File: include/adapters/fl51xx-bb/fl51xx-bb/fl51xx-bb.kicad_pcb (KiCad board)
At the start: 2 copper layers, 93.3 x 97.3 mm, 90 parts, among them J1 Conn_01x05, J2 Conn_01x05, U1 FL51xxMX

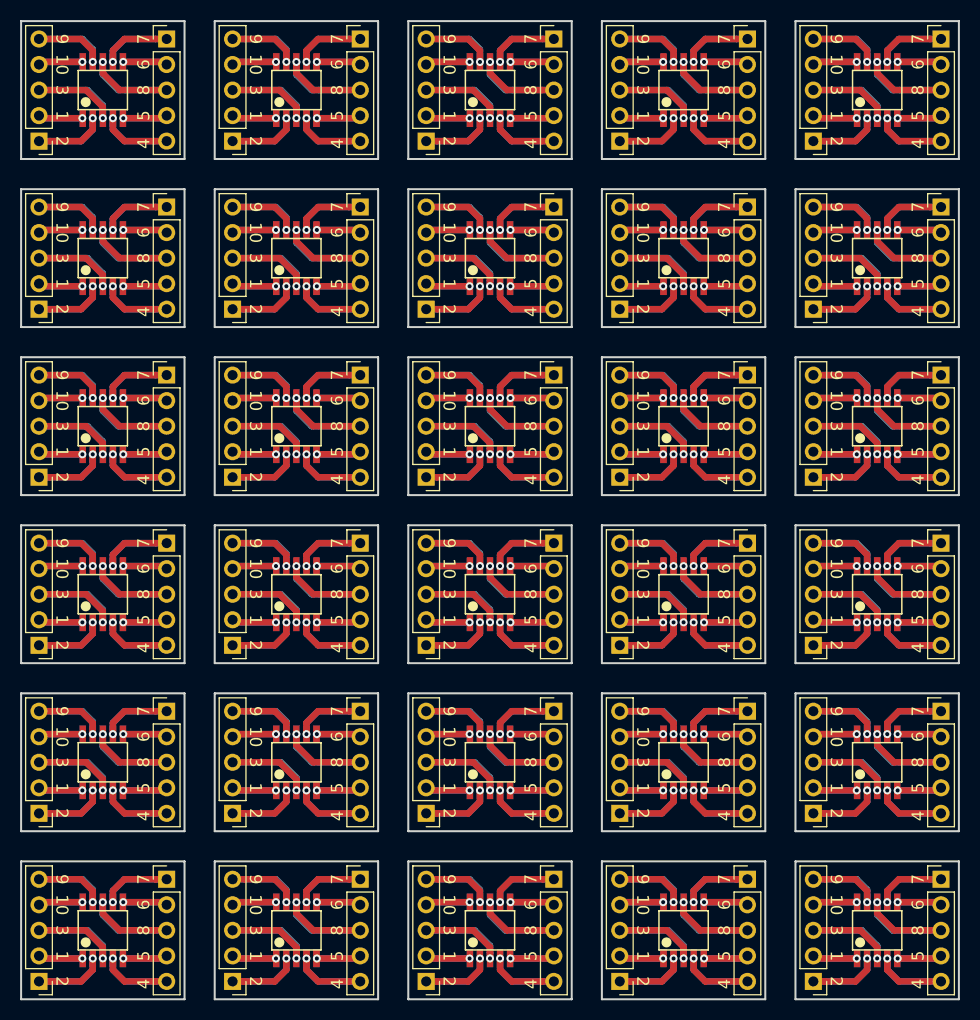
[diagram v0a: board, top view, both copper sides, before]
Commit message: removed duplicates
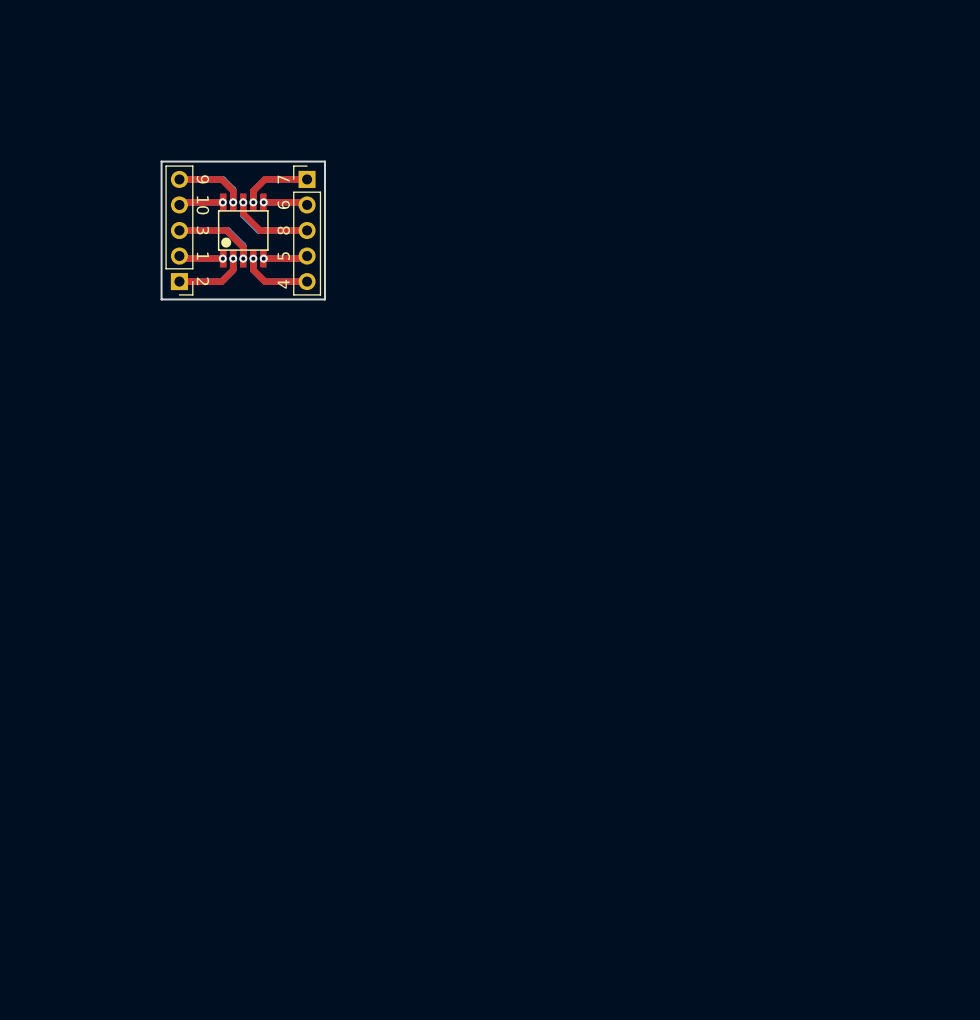
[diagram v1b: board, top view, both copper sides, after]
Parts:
- removed the J1 at (78.8, 95.5)
- removed the J1 at (1.78, 78.8)
- removed the J1 at (78.8, 62.1)
- removed the J1 at (59.5, 62.1)
- removed the J1 at (40.3, 62.1)
- removed the J1 at (21.0, 62.1)
- removed the J1 at (1.78, 62.1)
- removed the J1 at (78.8, 45.4)
- removed the J1 at (59.5, 45.4)
- removed the J1 at (40.3, 45.4)
- removed the J1 at (21.0, 45.4)
- removed the J1 at (59.5, 95.5)
- removed the J1 at (1.78, 45.4)
- removed the J1 at (78.8, 28.7)
- removed the J1 at (59.5, 28.7)
- removed the J1 at (40.3, 28.7)
- removed the J1 at (21.0, 28.7)
- removed the J1 at (1.78, 28.7)
- removed the J1 at (78.8, 11.9)
- removed the J1 at (59.5, 11.9)
- removed the J1 at (40.3, 11.9)
- removed the J1 at (21.0, 11.9)
- removed the J1 at (40.3, 95.5)
- removed the J1 at (21.0, 95.5)
- removed the J1 at (1.78, 95.5)
- removed the J1 at (78.8, 78.8)
- removed the J1 at (59.5, 78.8)
- removed the J1 at (40.3, 78.8)
- removed the J1 at (21.0, 78.8)
- removed the J2 at (91.5, 85.4)
- removed the J2 at (14.5, 68.6)
- removed the J2 at (91.5, 51.9)
- removed the J2 at (72.2, 51.9)
- removed the J2 at (53.0, 51.9)
- removed the J2 at (33.7, 51.9)
- removed the J2 at (14.5, 51.9)
- removed the J2 at (91.5, 35.2)
- removed the J2 at (72.2, 35.2)
- removed the J2 at (53.0, 35.2)
- removed the J2 at (33.7, 35.2)
- removed the J2 at (72.2, 85.4)
- removed the J2 at (14.5, 35.2)
- removed the J2 at (91.5, 18.5)
- removed the J2 at (72.2, 18.5)
- removed the J2 at (53.0, 18.5)
- removed the J2 at (33.7, 18.5)
- removed the J2 at (14.5, 18.5)
- removed the J2 at (91.5, 1.78)
- removed the J2 at (72.2, 1.78)
- removed the J2 at (53.0, 1.78)
- removed the J2 at (33.7, 1.78)
- removed the J2 at (53.0, 85.4)
- removed the J2 at (33.7, 85.4)
- removed the J2 at (14.5, 85.4)
- removed the J2 at (91.5, 68.6)
- removed the J2 at (72.2, 68.6)
- removed the J2 at (53.0, 68.6)
- removed the J2 at (33.7, 68.6)
- removed the U1 at (85.2, 90.4)
- removed the U1 at (8.13, 73.7)
- removed the U1 at (85.2, 57.0)
- removed the U1 at (65.9, 57.0)
- removed the U1 at (46.6, 57.0)
- removed the U1 at (27.4, 57.0)
- removed the U1 at (8.13, 57.0)
- removed the U1 at (85.2, 40.3)
- removed the U1 at (65.9, 40.3)
- removed the U1 at (46.6, 40.3)
- removed the U1 at (27.4, 40.3)
- removed the U1 at (65.9, 90.4)
- removed the U1 at (8.13, 40.3)
- removed the U1 at (85.2, 23.6)
- removed the U1 at (65.9, 23.6)
- removed the U1 at (46.6, 23.6)
- removed the U1 at (27.4, 23.6)
- removed the U1 at (8.13, 23.6)
- removed the U1 at (85.2, 6.86)
- removed the U1 at (65.9, 6.86)
- removed the U1 at (46.6, 6.86)
- removed the U1 at (27.4, 6.86)
- removed the U1 at (46.6, 90.4)
- removed the U1 at (27.4, 90.4)
- removed the U1 at (8.13, 90.4)
- removed the U1 at (85.2, 73.7)
- removed the U1 at (65.9, 73.7)
- removed the U1 at (46.6, 73.7)
- removed the U1 at (27.4, 73.7)
- moved J1 19.8 mm to (15.7, 25.9)
- moved J2 19.8 mm to (28.4, 15.7)
- moved U1 19.8 mm to (22.1, 20.8)
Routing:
- net Net-(J1-Pad3): track 516.2 -> 17.2 mm, vias 30 -> 1
- net Net-(J2-Pad3): track 492.6 -> 16.4 mm, vias 30 -> 1
- net Net-(J1-Pad5): track 419.4 -> 14.0 mm, vias 30 -> 1
- net Net-(J2-Pad5): track 417.2 -> 13.9 mm, vias 30 -> 1
- net Net-(J2-Pad1): track 417.2 -> 13.9 mm, vias 30 -> 1
- net Net-(J1-Pad1): track 417.2 -> 13.9 mm, vias 30 -> 1
- net Net-(J2-Pad4): track 266.5 -> 8.88 mm, vias 30 -> 1
- net Net-(J1-Pad2): track 266.5 -> 8.88 mm, vias 30 -> 1
- net Net-(J1-Pad4): track 266.5 -> 8.88 mm, vias 30 -> 1
- net Net-(J2-Pad2): track 266.5 -> 8.88 mm, vias 30 -> 1
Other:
- board size 93.3 x 97.3 mm -> 16.3 x 13.7 mm

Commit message: first order
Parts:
- added J10: Conn_01x01, Connector_PinHeader_2.54mm:PinHeader_1x01_P2.54mm_Vertical, F.Cu at (31.5, 20.1)
- added J3: Conn_01x01, Connector_PinHeader_2.54mm:PinHeader_1x01_P2.54mm_Vertical, F.Cu at (18.8, 22.6)
- added J4: Conn_01x01, Connector_PinHeader_2.54mm:PinHeader_1x01_P2.54mm_Vertical, F.Cu at (31.5, 27.7)
- added J5: Conn_01x01, Connector_PinHeader_2.54mm:PinHeader_1x01_P2.54mm_Vertical, F.Cu at (31.5, 25.1)
- added J6: Conn_01x01, Connector_PinHeader_2.54mm:PinHeader_1x01_P2.54mm_Vertical, F.Cu at (18.8, 20.1)
- added J7: Conn_01x01, Connector_PinHeader_2.54mm:PinHeader_1x01_P2.54mm_Vertical, F.Cu at (18.8, 17.5)
- added J8: Conn_01x01, Connector_PinHeader_2.54mm:PinHeader_1x01_P2.54mm_Vertical, F.Cu at (31.5, 22.6)
- added J9: Conn_01x01, Connector_PinHeader_2.54mm:PinHeader_1x01_P2.54mm_Vertical, F.Cu at (31.5, 17.5)
- J1, J2: value Conn_01x05 -> Conn_01x01; footprint Connector_PinHeader_2.54mm:PinHeader_1x05_P2.54mm_Vertical -> Connector_PinHeader_2.54mm:PinHeader_1x01_P2.54mm_Vertical
- moved J2 15.4 mm to (18.8, 27.7)
- moved U1 3.53 mm to (25.1, 22.6)
- moved J1 3.14 mm to (18.8, 25.1), turned to 0 degrees
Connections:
- U1 pad 1: Net-(J1-Pad2) -> Net-(J1-Pad1)
- U1 pad 10: Net-(J1-Pad4) -> Net-(J6-Pad1)
- U1 pad 2: Net-(J1-Pad1) -> Net-(J2-Pad1)
- U1 pad 3: Net-(J1-Pad3) -> Net-(J3-Pad1)
- U1 pad 4: Net-(J2-Pad5) -> Net-(J4-Pad1)
- U1 pad 5: Net-(J2-Pad4) -> Net-(J5-Pad1)
- U1 pad 6: Net-(J2-Pad2) -> Net-(J10-Pad1)
- U1 pad 7: Net-(J2-Pad1) -> Net-(J9-Pad1)
- U1 pad 8: Net-(J2-Pad3) -> Net-(J8-Pad1)
- U1 pad 9: Net-(J1-Pad5) -> Net-(J7-Pad1)
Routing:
- net Net-(J3-Pad1): track 0.00 -> 17.3 mm, vias 0 -> 1
- net Net-(J1-Pad3): track 17.2 -> 0.00 mm, vias 1 -> 0
- net Net-(J8-Pad1): track 0.00 -> 16.5 mm, vias 0 -> 1
- net Net-(J2-Pad3): track 16.4 -> 0.00 mm, vias 1 -> 0
- net Net-(J7-Pad1): track 0.00 -> 15.0 mm, vias 0 -> 1
- net Net-(J1-Pad5): track 14.0 -> 0.00 mm, vias 1 -> 0
- net Net-(J2-Pad5): track 13.9 -> 0.00 mm, vias 1 -> 0
- net Net-(J9-Pad1): track 0.00 -> 13.9 mm, vias 0 -> 1
- net Net-(J4-Pad1): track 0.00 -> 13.9 mm, vias 0 -> 1
- net Net-(J2-Pad4): track 8.88 -> 0.00 mm, vias 1 -> 0
- net Net-(J2-Pad2): track 8.88 -> 0.00 mm, vias 1 -> 0
- net Net-(J1-Pad4): track 8.88 -> 0.00 mm, vias 1 -> 0
- net Net-(J1-Pad2): track 8.88 -> 0.00 mm, vias 1 -> 0
- net Net-(J6-Pad1): track 0.00 -> 8.88 mm, vias 0 -> 1
- net Net-(J5-Pad1): track 0.00 -> 8.88 mm, vias 0 -> 1
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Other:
- board text added: "SOIC12 breadboard adapter"
- board text removed: "FL51xx breadboard adapter"
